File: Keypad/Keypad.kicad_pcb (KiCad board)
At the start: 2 copper layers, 50 x 35 mm, 17 parts, among them J1 locked, SW1 TL1240GQ1JCLR, SW2 TL1240GQ1JCLR, SW3 TL1240GQ1JCLR, SW4 TL1240GQ1JCLR, SW5 TL1240GQ1JCLR, SW6 TL1240GQ1JCLR

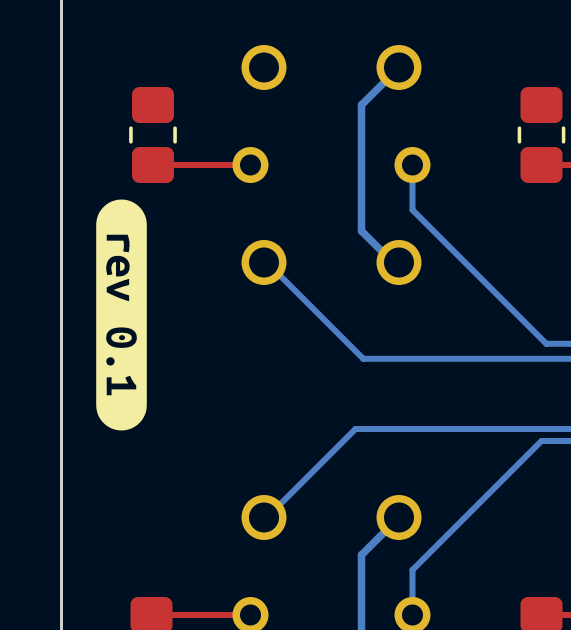
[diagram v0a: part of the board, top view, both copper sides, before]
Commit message: Update version label on PCBs to 1.0
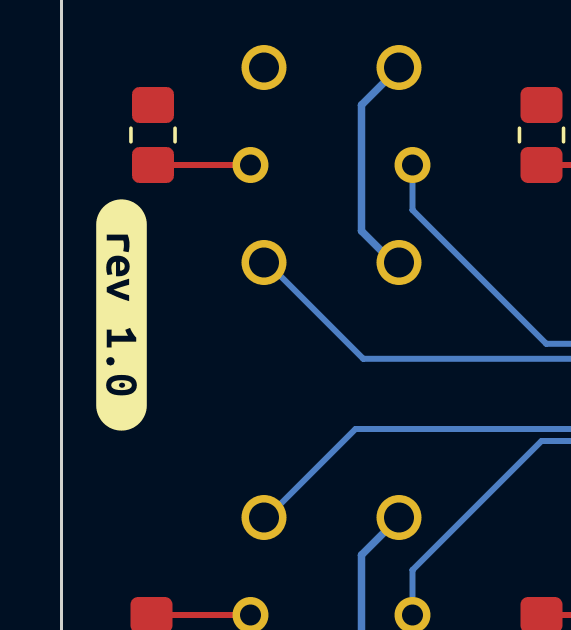
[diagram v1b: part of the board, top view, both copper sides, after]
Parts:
- removed kibuzzard-6290844C: G***, kibuzzard-6290844C
- added kibuzzard-63029D1F: G***, kibuzzard-63029D1F, F.Cu at (122.0, 97.0)
